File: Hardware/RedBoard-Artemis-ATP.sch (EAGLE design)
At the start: 81 parts, among them IC3 LM1117, J2 CORTEX_DEBUG, J3 POWER_JACKTOE, J5 USB-C, Q1 1.1A/60V/600mΩ, U3 AP2112-3.3V, U4 ARTEMIS_MODULESMD, U5 CH340C, Y1 32.768kHz

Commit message: Add SMD Debug. Add PTH holes to each connector.
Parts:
- removed D5: 1A/23V/620mV, SparkFun-DiscreteSemi:DIODE-SCHOTTKY-BAT20J
- added J8: (no value), SparkFun-Connectors:CONN_05NO_SILK
- added JP12, JP25, JP26: JP11, SparkFun-Connectors:M08NO_SILK
- added JP23: M10NO_SILK, SparkFun-Connectors:M10NO_SILK
- added JP24: (no value), SparkFun-Connectors:M08NO_SILK
- added MEAS: JUMPER-SMT_2_NC_TRACE_SILK, SparkFun-Jumpers:JUMPER-SMT_2_NC_TRACE_SILK
- D4: value 1A/23V/620mV -> 3A/10V/280mV; device SparkFun-DiscreteSemi:DIODE-SCHOTTKY-BAT20J -> SparkFun-DiscreteSemi:DIODE-SCHOTTKY-BAT60A
- J2: device SparkFun-Connectors:CORTEX_DEBUG_MINIMUM_PTH_NS -> SparkFun-Connectors:CORTEX_JTAG_DEBUG_MINIMUM_SMD
- J5: device SparkFun-Connectors:USB_C -> SparkFun-Connectors:USB_C2-LAYER
- JP15: value JUMPER-SMT_2_NC_TRACE_SILK -> JP11; device SparkFun-Jumpers:JUMPER-SMT_2_NC_TRACE_SILK -> SparkFun-Connectors:M08NO_SILK; PROD_ID (none) -> CONN-10204
- Q1: value 1.1A/60V/600mΩ -> 2.5A/30V/105mΩ; device SparkFun-DiscreteSemi:MOSFET_PCH-SI2309DS -> SparkFun-DiscreteSemi:MOSFET_PCH-DMG2307L
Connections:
- removed net N$3: D4.C, D5.C, J1.2, JP15.1
- net !RESET: now also JP24.6
- net 3.3V: now also D4.C, J1.2, MEAS.1; no longer D5.A
- net 5V: now also JP24.4
- net AD16: now also JP26.5
- net AD34: now also JP26.3
- net D0: now also JP15.6
- net D1: now also JP15.5
- net D10: now also JP12.3
- net D14: now also JP12.1
- net D15: now also JP12.6
- net D17: now also JP15.1
- net D2: now also JP15.4
- net D40/SDA: now also JP23.2
- net D41: now also JP15.2
- net D8: now also JP12.2
- net D9: now also JP12.4
- net GND: now also J8.1, J8.2, J8.3, J8.4, J8.5, JP13.7, JP13.8, JP23.3, JP23.4, JP24.2, JP24.3, JP26.7, JP26.8
- net VDD: now also JP24.5, JP24.7, MEAS.2; no longer JP15.2
- net VIN: now also JP24.1
- net ~AD11: now also JP26.2
- net ~AD12: now also JP23.9
- net ~AD13: now also JP23.8
- net ~AD29: now also JP26.1
- net ~AD31: now also JP26.6
- net ~AD32: now also JP23.10
- net ~AD33/SWO: now also JP26.4
- net ~AD35: now also JP25.3
- net ~D18: now also JP12.8
- net ~D19: now also JP12.7
- net ~D22: now also JP25.5
- net ~D23: now also JP25.6
- net ~D24/TXO-1: now also JP25.2
- net ~D25/RXI-1: now also JP25.1
- net ~D26: now also JP12.5
- net ~D27: now also JP25.7
- net ~D28: now also JP25.8
- net ~D39/SCL: now also JP23.1
- net ~D4: now also JP25.4
- net ~D42: now also JP15.8
- net ~D43: now also JP15.7
- net ~D45: now also JP15.3
- net ~D5/SCK: now also JP23.5
- net ~D6/MISO: now also JP23.6
- net ~D7/MOSI: now also JP23.7
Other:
- note added: "PTH Connections"

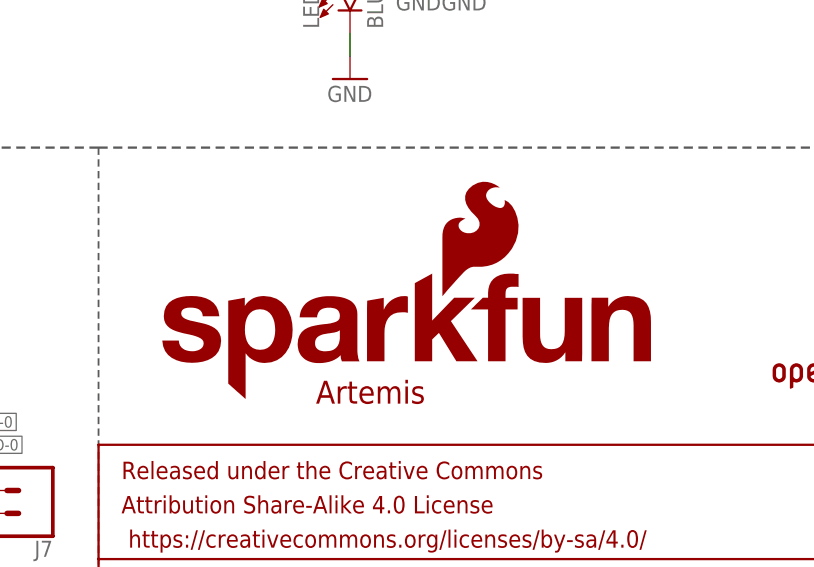
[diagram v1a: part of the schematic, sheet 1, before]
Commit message: Add silk indicators to PTH pins
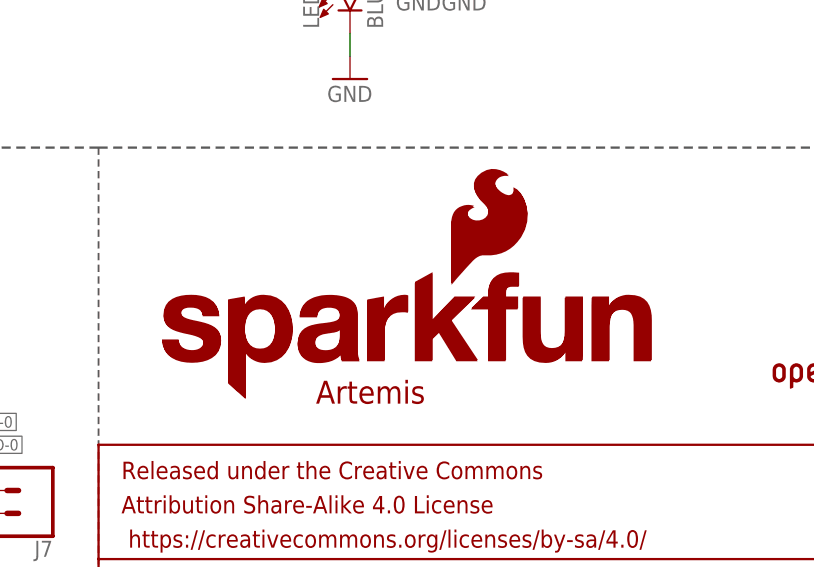
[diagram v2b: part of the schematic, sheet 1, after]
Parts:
- added LOGO1: SFE_LOGO_NAME_FLAME.1_INCH, SparkFun-Aesthetics:SFE_LOGO_NAME_FLAME.1_INCH
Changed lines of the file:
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@@
 <grid distance="0.1" unitdist="inch" unit="inch" style="lines" multiple="1" display="no" altdistance="0.01" altunitdist="inch" altunit="inch"/>
 <layers>
-<layer number="1" name="Top" color="4" fill="1" visible="yes" active="no"/>
-<layer number="2" name="Route2" color="1" fill="3" visible="yes" active="no"/>
-<layer number="3" name="Route3" color="4" fill="3" visible="yes" active="no"/>
-<layer number="4" name="Route4" color="1" fill="4" visible="yes" active="no"/>
-<layer number="5" name="Route5" color="4" fill="4" visible="yes" active="no"/>
-<layer number="6" name="Route6" color="1" fill="8" visible="yes" active="no"/>
-<layer number="7" name="Route7" color="4" fill="8" visible="yes" active="no"/>
-<layer number="8" name="Route8" color="1" fill="2" visible="yes" active="no"/>
-<layer number="9" name="Route9" color="4" fill="2" visible="yes" active="no"/>
-<layer number="10" name="Route10" color="1" fill="7" visible="yes" active="no"/>
-<layer number="11" name="Route11" color="4" fill="7" visible="yes" active="no"/>
-<layer number="12" name="Route12" color="1" fill="5" visible="yes" active="no"/>
-<layer number="13" name="Route13" color="4" fill="5" visible="yes" active="no"/>
-<layer number="14" name="Route14" color="1" fill="6" visible="yes" active="no"/>
-<layer number="15" name="Route15" color="4" fill="6" visible="yes" active="no"/>
-<layer number="16" name="Bottom" color="1" fill="1" visible="yes" active="no"/>
-<layer number="17" name="Pads" color="2" fill="1" visible="yes" active="no"/>
-<layer number="18" name="Vias" color="2" fill="1" visible="yes" active="no"/>
-<layer number="19" name="Unrouted" color="6" fill="1" visible="yes" active="no"/>
-<layer number="20" name="Dimension" color="24" fill="1" visible="yes" active="no"/>
-<layer number="21" name="tPlace" color="16" fill="1" visible="yes" active="no"/>
-<layer number="22" name="bPlace" color="14" fill="1" visible="yes" active="no"/>
-<layer number="23" name="tOrigins" color="15" fill="1" visible="yes" active="no"/>
-<layer number="24" name="bOrigins" color="15" fill="1" visible="yes" active="no"/>
-<layer number="25" name="tNames" color="7" fill="1" visible="yes" active="no"/>
-<layer number="26" name="bNames" color="7" fill="1" visible="yes" active="no"/>
-<layer number="27" name="tValues" color="7" fill="1" visible="yes" active="no"/>
-<layer number="28" name="bValues" color="7" fill="1" visible="yes" active="no"/>
+<layer number="1" name="Top" color="4" fill="1" visible="no" active="no"/>
+<layer number="2" name="Route2" color="1" fill="3" visible="no" active="no"/>
+<layer number="3" name="Route3" color="4" fill="3" visible="no" active="no"/>
+<layer number="4" name="Route4" color="1" fill="4" visible="no" active="no"/>
+<layer number="5" name="Route5" color="4" fill="4" visible="no" active="no"/>
+<layer number="6" name="Route6" color="1" fill="8" visible="no" active="no"/>
+<layer number="7" name="Route7" color="4" fill="8" visible="no" active="no"/>
+<layer number="8" name="Route8" color="1" fill="2" visible="no" active="no"/>
+<layer number="9" name="Route9" color="4" fill="2" visible="no" active="no"/>
+<layer number="10" name="Route10" color="1" fill="7" visible="no" active="no"/>
+<layer number="11" name="Route11" color="4" fill="7" visible="no" active="no"/>
+<layer number="12" name="Route12" color="1" fill="5" visible="no" active="no"/>
+<layer number="13" name="Route13" color="4" fill="5" visible="no" active="no"/>
+<layer number="14" name="Route14" color="1" fill="6" visible="no" active="no"/>
+<layer number="15" name="Route15" color="4" fill="6" visible="no" active="no"/>
+<layer number="16" name="Bottom" color="1" fill="1" visible="no" active="no"/>
+<layer number="17" name="Pads" color="2" fill="1" visible="no" active="no"/>
+<layer number="18" name="Vias" color="2" fill="1" visible="no" active="no"/>
+<layer number="19" name="Unrouted" color="6" fill="1" visible="no" active="no"/>
+<layer number="20" name="Dimension" color="24" fill="1" visible="no" active="no"/>
+<layer number="21" name="tPlace" color="16" fill="1" visible="no" active="no"/>
+<layer number="22" name="bPlace" color="14" fill="1" visible="no" active="no"/>
+<layer number="23" name="tOrigins" color="15" fill="1" visible="no" active="no"/>
+<layer number="24" name="bOrigins" color="15" fill="1" visible="no" active="no"/>
+<layer number="25" name="tNames" color="7" fill="1" visible="no" active="no"/>
+<layer number="26" name="bNames" color="7" fill="1" visible="no" active="no"/>
+<layer number="27" name="tValues" color="7" fill="1" visible="no" active="no"/>
+<layer number="28" name="bValues" color="7" fill="1" visible="no" active="no"/>
 <layer number="29" name="tStop" color="2" fill="3" visible="no" active="no"/>
 <layer number="30" name="bStop" color="5" fill="6" visible="no" active="no"/>
@@
 <layer number="35" name="tGlue" color="7" fill="4" visible="no" active="no"/>
 <layer number="36" name="bGlue" color="7" fill="5" visible="no" active="no"/>
-<layer number="37" name="tTest" color="7" fill="1" visible="yes" active="no"/>
-<layer number="38" name="bTest" color="7" fill="1" visible="yes" active="no"/>
+<layer number="37" name="tTest" color="7" fill="1" visible="no" active="no"/>
+<layer number="38" name="bTest" color="7" fill="1" visible="no" active="no"/>
 <layer number="39" name="tKeepout" color="4" fill="11" visible="no" active="no"/>
 <layer number="40" name="bKeepout" color="1" fill="11" visible="no" active="no"/>
@@
 <layer number="44" name="Drills" color="7" fill="1" visible="no" active="no"/>
 <layer number="45" name="Holes" color="7" fill="1" visible="no" active="no"/>
-<layer number="46" name="Milling" color="3" fill="1" visible="yes" active="no"/>
-<layer number="47" name="Measures" color="7" fill="1" visible="yes" active="no"/>
-<layer number="48" name="Document" color="7" fill="1" visible="yes" active="no"/>
-<layer number="49" name="Reference" color="13" fill="1" visible="yes" active="no"/>
-<layer number="50" name="dxf" color="12" fill="1" visible="yes" active="no"/>
-<layer number="51" name="tDocu" color="6" fill="1" visible="yes" active="no"/>
-<layer number="52" name="bDocu" color="7" fill="1" visible="yes" active="no"/>
-<layer number="53" name="tGND_GNDA" color="7" fill="1" visible="yes" active="no"/>
-<layer number="54" name="bGND_GNDA" color="7" fill="1" visible="yes" active="no"/>
-<layer number="56" name="wert" color="7" fill="1" visible="yes" active="no"/>
-<layer number="57" name="tCAD" color="7" fill="1" visible="yes" active="no"/>
-<layer number="59" name="tCarbon" color="7" fill="1" visible="yes" active="no"/>
-<layer number="60" name="bCarbon" color="7" fill="1" visible="yes" active="no"/>
+<layer number="46" name="Milling" color="3" fill="1" visible="no" active="no"/>
+<layer number="47" name="Measures" color="7" fill="1" visible="no" active="no"/>
+<layer number="48" name="Document" color="7" fill="1" visible="no" active="no"/>
+<layer number="49" name="Reference" color="13" fill="1" visible="no" active="no"/>
+<layer number="50" name="dxf" color="12" fill="1" visible="no" active="no"/>
+<layer number="51" name="tDocu" color="6" fill="1" visible="no" active="no"/>
+<layer number="52" name="bDocu" color="7" fill="1" visible="no" active="no"/>
+<layer number="53" name="tGND_GNDA" color="7" fill="1" visible="no" active="no"/>
+<layer number="54" name="bGND_GNDA" color="7" fill="1" visible="no" active="no"/>
+<layer number="56" name="wert" color="7" fill="1" visible="no" active="no"/>
+<layer number="57" name="tCAD" color="7" fill="1" visible="no" active="no"/>
+<layer number="59" name="tCarbon" color="7" fill="1" visible="no" active="no"/>
+<layer number="60" name="bCarbon" color="7" fill="1" visible="no" active="no"/>
 <layer number="88" name="SimResults" color="9" fill="1" visible="yes" active="yes"/>
 <layer number="89" name="SimProbes" color="9" fill="1" visible="yes" active="yes"/>
@@
 </part>
 <part name="GND39" library="SparkFun-PowerSymbols" deviceset="GND" device=""/>
+<part name="LOGO1" library="SparkFun-Aesthetics" deviceset="SFE_LOGO_NAME_FLAME" device=".1_INCH"/>
 </parts>
 <sheets>
@@
 </instance>
 <instance part="JP1" gate="G$1" x="152.4" y="40.64" smashed="yes"/>
-<instance part="JP7" gate="G$1" x="185.166" y="51.562" smashed="yes"/>
+<instance part="JP7" gate="G$1" x="186.182" y="52.832" smashed="yes"/>
 <instance part="GND10" gate="1" x="68.58" y="10.16" smashed="yes">
 <attribute name="VALUE" x="66.04" y="7.62" size="1.778" layer="96"/>
@@
 <attribute name="VALUE" x="45.72" y="86.36" size="1.778" layer="96"/>
 </instance>
+<instance part="LOGO1" gate="G$1" x="153.67" y="40.386" smashed="yes"/>
 </instances>
 <busses>

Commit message: Consolidated to one sch sheet.
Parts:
- removed FRAME1: FRAME-LETTER, SparkFun-Aesthetics:FRAME-LETTER
- removed FRAME2: FRAME-LETTERNO_PACKAGE, SparkFun-Aesthetics:FRAME-LETTERNO_PACKAGE
- removed J6, J8: (no value), SparkFun-Connectors:CONN_05NO_SILK
- removed JP15: JP11, SparkFun-Connectors:M08NO_SILK
- removed MEAS: JUMPER-SMT_2_NC_TRACE_SILK, SparkFun-Jumpers:JUMPER-SMT_2_NC_TRACE_SILK
- added FRAME3: FRAME-LEDGER, SparkFun-Aesthetics:FRAME-LEDGER
- added JP27, JP28, JP29: (no value), SparkFun-Connectors:CONN_08NO_SILK_FEMALE_PTH
- added JP30: (no value), SparkFun-Connectors:CONN_05NO_SILK
- JP11, JP13, JP19, JP20: value JP11 -> (none); device SparkFun-Connectors:M08SMD-COMBO -> SparkFun-Connectors:CONN_08SMD-COMBO-FEMALE_NC; PROD_ID CONN-10204 -> (none)
- JP12: value JP11 -> MEAS; device SparkFun-Connectors:M08NO_SILK -> SparkFun-Jumpers:JUMPER-SMT_2_NC_TRACE_SILK; PROD_ID CONN-10204 -> (none)
- JP2: value M10SMD_COMBO -> (none); device SparkFun-Connectors:M10SMD_COMBO -> SparkFun-Connectors:CONN_10SMD_COMBO-FEMALE
- JP25: value JP11 -> (none); device SparkFun-Connectors:M08NO_SILK -> SparkFun-Connectors:CONN_05NO_SILK; PROD_ID CONN-10204 -> (none)
- JP26: value JP11 -> (none); device SparkFun-Connectors:M08NO_SILK -> SparkFun-Connectors:CONN_08NO_SILK_FEMALE_PTH; PROD_ID CONN-10204 -> (none)
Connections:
- net USBVCC renamed V_USB
- net 3.3V: now also JP12.1; no longer MEAS.1
- net AD16: now also JP27.5; no longer JP26.5
- net AD34: now also JP27.3; no longer JP26.3
- net D0: now also JP29.6; no longer JP15.6
- net D1: now also JP29.5; no longer JP15.5
- net D10: now also JP28.6; no longer JP12.3
- net D14: now also JP28.8; no longer JP12.1
- net D15: now also JP28.3; no longer JP12.6
- net D17: now also JP29.1; no longer JP15.1
- net D2: now also JP29.4; no longer JP15.4
- net D3: now also JP25.1; no longer J6.1
- net D36: now also JP25.2; no longer J6.2
- net D38: now also JP25.3; no longer J6.3
- net D41: now also JP29.2; no longer JP15.2
- net D8: now also JP28.7; no longer JP12.2
- net D9: now also JP28.5; no longer JP12.4
- net GND: now also JP27.7, JP27.8, JP30.1, JP30.2, JP30.3, JP30.4, JP30.5; no longer J8.1, J8.2, J8.3, J8.4, J8.5, JP26.7, JP26.8
- net VDD: now also JP12.2; no longer MEAS.2
- net ~AD11: now also JP27.2; no longer JP26.2
- net ~AD29: now also JP27.1; no longer JP26.1
- net ~AD31: now also JP27.6; no longer JP26.6
- net ~AD33/SWO: now also JP27.4; no longer JP26.4
- net ~AD35: now also JP26.3; no longer JP25.3
- net ~D18: now also JP28.1; no longer JP12.8
- net ~D19: now also JP28.2; no longer JP12.7
- net ~D22: now also JP26.5; no longer JP25.5
- net ~D23: now also JP26.6; no longer JP25.6
- net ~D24/TXO-1: now also JP26.2; no longer JP25.2
- net ~D25/RXI-1: now also JP26.1; no longer JP25.1
- net ~D26: now also JP28.4; no longer JP12.5
- net ~D27: now also JP26.7; no longer JP25.7
- net ~D28: now also JP26.8; no longer JP25.8
- net ~D37: now also JP25.4; no longer J6.4
- net ~D4: now also JP26.4; no longer JP25.4
- net ~D42: now also JP29.8; no longer JP15.8
- net ~D43: now also JP29.7; no longer JP15.7
- net ~D44: now also JP25.5; no longer J6.5
- net ~D45: now also JP29.3; no longer JP15.3
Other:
- note added: "SMD Connectors"
- note added: "V10"
- note removed: "Artemis Decoupling"
- note removed: "X02"
- moved on the sheet: BYP, C10, C11, C12, C13, C15, C17, C18, D2, D3, F2, J5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

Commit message: Adding production panels
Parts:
- U4: device Testing:ARTEMIS_MODULESMD -> SparkFun-IC-Microcontroller:ARTEMIS_MODULESMD
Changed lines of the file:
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@@
 <part name="JP21" library="SparkFun-Jumpers" deviceset="JUMPER-SMT_2_NC_TRACE" device="_SILK" value=""/>
 <part name="JP22" library="SparkFun-Jumpers" deviceset="JUMPER-SMT_2_NC_TRACE" device="_SILK" value=""/>
-<part name="U4" library="Testing" deviceset="ARTEMIS_MODULE" device="SMD"/>
+<part name="U4" library="SparkFun-IC-Microcontroller" deviceset="ARTEMIS_MODULE" device="SMD"/>
 <part name="LOGO1" library="SparkFun-Aesthetics" deviceset="SFE_LOGO_NAME_FLAME" device=".1_INCH"/>
 <part name="SUPPLY27" library="SparkFun-PowerSymbols" deviceset="V_USB" device=""/>
